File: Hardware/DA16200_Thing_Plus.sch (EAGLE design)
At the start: 60 parts, among them J2 THING_PLUS, J3 Qwiic, J5 USB C, J6 microSD, J7 CORTEX_JTAG_DEBUG_PTH_NS, Q1 20V/4.2A/52mΩ/1.4W, U1 DA16200MOD, U2 CH340E_MSOP10, U3 MCP73831, U7 3.3V

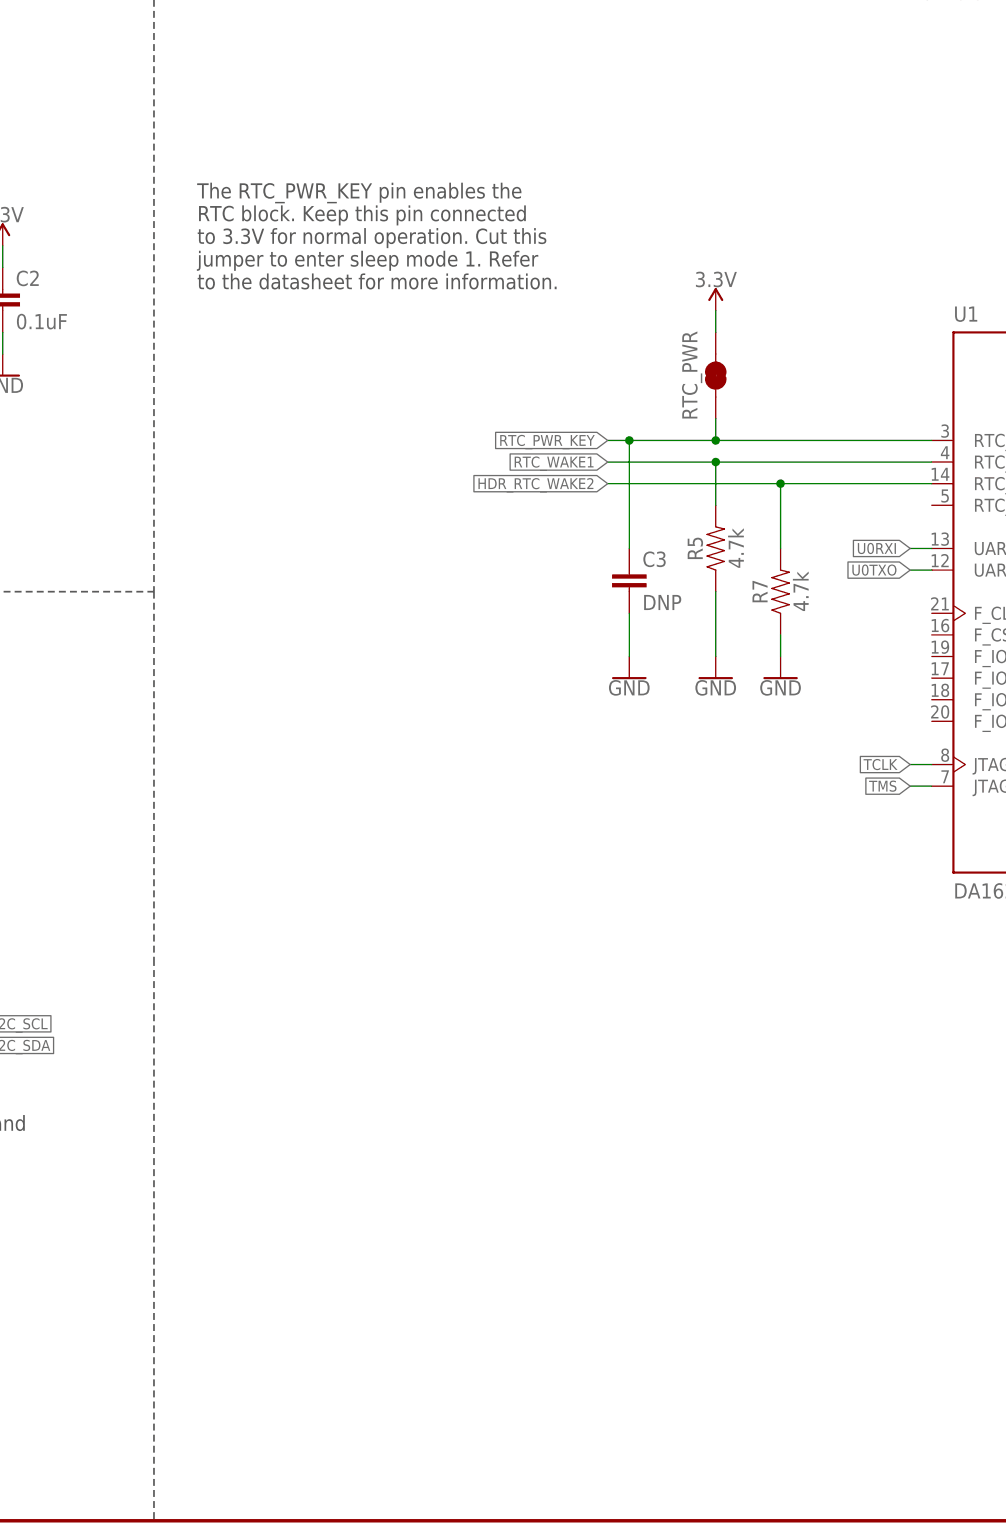
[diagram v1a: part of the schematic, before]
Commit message: Add SPDT switch for RTC_PWR_KEY
Added surface mount switch to pull RTC_PWR_KEY to 3.3V or GND
* Needed to extend the length of board by one grid space
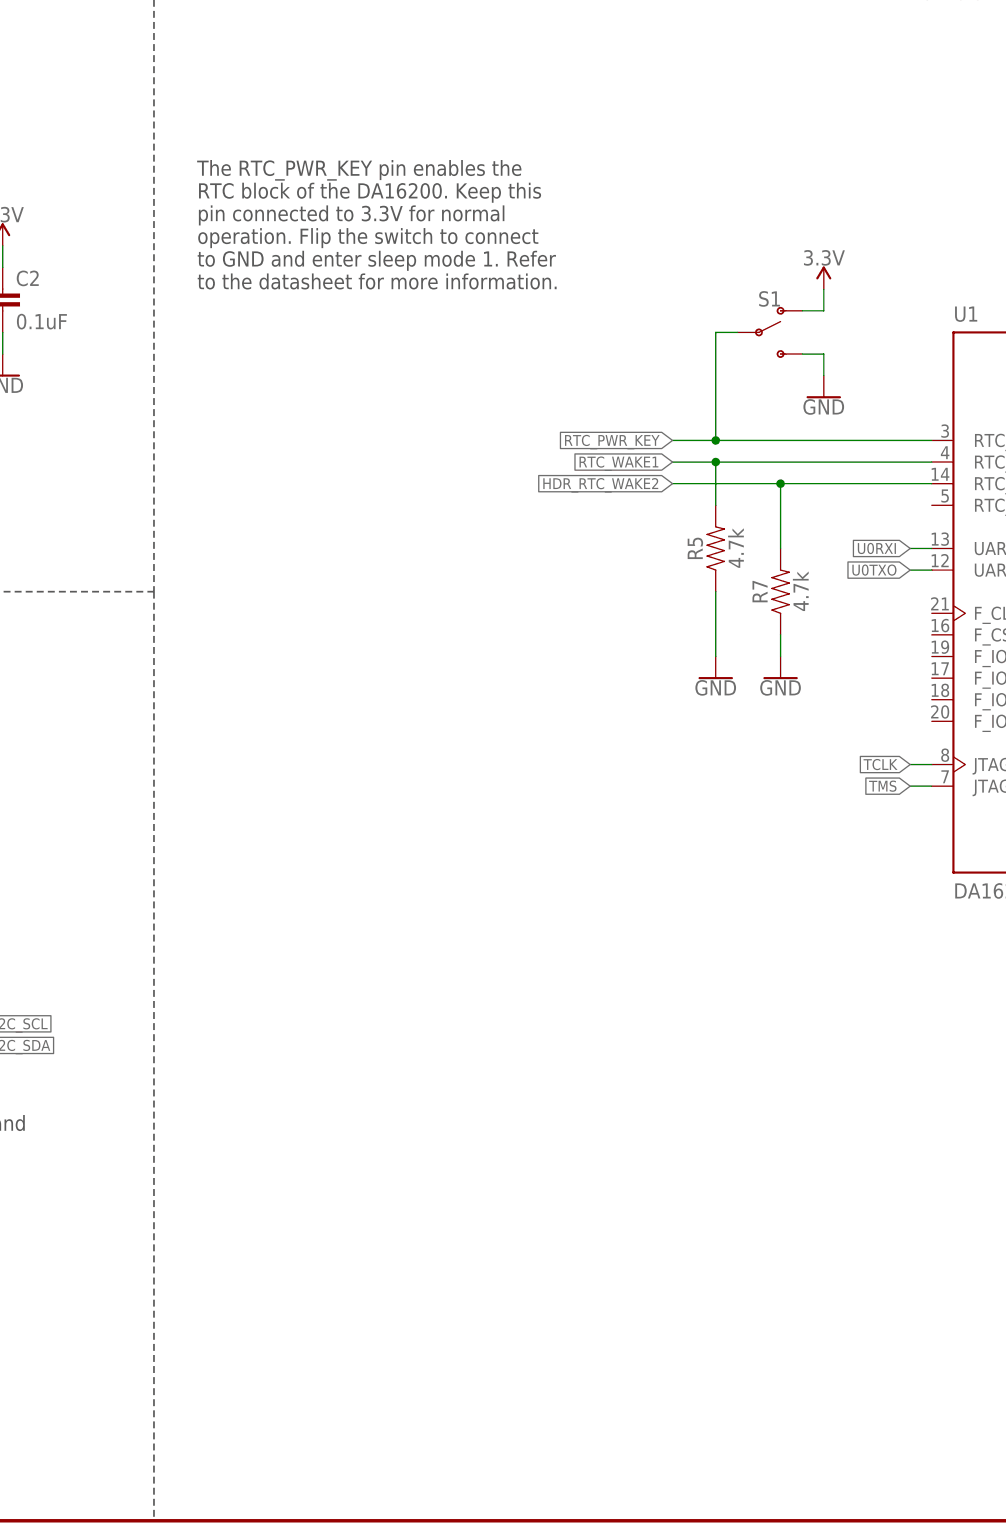
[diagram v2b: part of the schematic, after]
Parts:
- removed C3: DNP, SparkFun-Capacitors:DNP-0402-TIGHT
- removed RTC_PWR: JUMPER-SMT_2_NC_TRACE_SILK, SparkFun-Jumpers:JUMPER-SMT_2_NC_TRACE_SILK
- added S1: (no value), SparkFun-Switches:SWITCH-SPDT-SMD-AYZ0202
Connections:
- net 3.3V: now also S1.O; no longer RTC_PWR.2
- net GND: now also S1.S; no longer C3.2
- net RTC_PWR_KEY: now also S1.P; no longer C3.1, RTC_PWR.1
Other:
- note added: "The RTC_PWR_KEY pin enables the RTC block of the DA16200. Keep this pin connected to 3.3V for normal operation. Flip the switch to connect to GND and enter sleep mode 1. Refer to the datasheet for more information."
- note removed: "The RTC_PWR_KEY pin enables the RTC block. Keep this pin connected to 3.3V for normal operation. Cut this jumper to enter sleep mode 1. Refer to the datasheet for more information."
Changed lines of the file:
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@@
 <part name="R5" library="SparkFun-Resistors" deviceset="4.7KOHM" device="-0402T-1/16W-1%" value="4.7k"/>
 <part name="R7" library="SparkFun-Resistors" deviceset="4.7KOHM" device="-0402T-1/16W-1%" value="4.7k"/>
-<part name="C3" library="SparkFun-Capacitors" deviceset="DNP" device="-0402-TIGHT" value="DNP"/>
 <part name="GND17" library="SparkFun-PowerSymbols" deviceset="GND" device=""/>
 <part name="GND18" library="SparkFun-PowerSymbols" deviceset="GND" device=""/>
@@
 <part name="TMS" library="SparkFun-Connectors" deviceset="TEST-POINT" device="3"/>
 <part name="GPIOC7" library="SparkFun-Connectors" deviceset="TEST-POINT" device="3"/>
-<part name="RTC_PWR" library="SparkFun-Jumpers" deviceset="JUMPER-SMT_2_NC_TRACE" device="_SILK" package3d_urn="urn:adsk.eagle:package:39281/1"/>
+<part name="S1" library="SparkFun-Switches" deviceset="SWITCH-SPDT" device="-SMD-AYZ0202"/>
 </parts>
 <sheets>
@@
 <wire x1="261.62" y1="137.16" x2="330.2" y2="137.16" width="0.2032" layer="97" style="longdash"/>
 <wire x1="76.2" y1="190.5" x2="76.2" y2="109.22" width="0.2032" layer="97" style="longdash"/>
-<wire x1="76.2" y1="109.22" x2="76.2" y2="66.04" width="0.2032" layer="97" style="longdash"/>
-<wire x1="76.2" y1="66.04" x2="76.2" y2="0" width="0.2032" layer="97" style="longdash"/>
+<wire x1="76.2" y1="109.22" x2="76.2" y2="0" width="0.2032" layer="97" style="longdash"/>
 <wire x1="0" y1="109.22" x2="76.2" y2="109.22" width="0.2032" layer="97" style="longdash"/>
 <text x="172.974" y="180.086" size="2.54" layer="94" font="vector" align="center">DA16200 Module</text>
@@
 from power.</text>
 <text x="81.28" y="144.78" size="1.778" layer="97" font="vector">The RTC_PWR_KEY pin enables the
-RTC block. Keep this pin connected
-to 3.3V for normal operation. Cut this
-jumper to enter sleep mode 1. Refer
+RTC block of the DA16200. Keep this
+pin connected to 3.3V for normal
+operation. Flip the switch to connect
+to GND and enter sleep mode 1. Refer
 to the datasheet for more information.</text>
 </plain>
@@
 <attribute name="VALUE" x="151.384" y="109.22" size="1.778" layer="96" font="vector" rot="R90" align="top-center"/>
 </instance>
-<instance part="C3" gate="G$1" x="132.08" y="109.22" smashed="yes">
-<attribute name="NAME" x="133.604" y="112.141" size="1.778" layer="95" font="vector"/>
-<attribute name="VALUE" x="133.604" y="107.061" size="1.778" layer="96" font="vector"/>
-</instance>
-<instance part="GND17" gate="1" x="132.08" y="99.06" smashed="yes">
-<attribute name="VALUE" x="132.08" y="98.806" size="1.778" layer="96" align="top-center"/>
+<instance part="GND17" gate="1" x="154.94" y="132.08" smashed="yes">
+<attribute name="VALUE" x="154.94" y="131.826" size="1.778" layer="96" align="top-center"/>
 </instance>
 <instance part="GND18" gate="1" x="142.24" y="99.06" smashed="yes">
@@
 <attribute name="VALUE" x="149.86" y="98.806" size="1.778" layer="96" align="top-center"/>
 </instance>
-<instance part="SUPPLY8" gate="G$1" x="142.24" y="142.24" smashed="yes">
-<attribute name="VALUE" x="142.24" y="145.034" size="1.778" layer="96" align="bottom-center"/>
+<instance part="SUPPLY8" gate="G$1" x="154.94" y="144.78" smashed="yes">
+<attribute name="VALUE" x="154.94" y="147.574" size="1.778" layer="96" align="bottom-center"/>
 </instance>
 <instance part="LED" gate="G$1" x="281.94" y="109.22" smashed="yes" rot="R90">
@@
 <attribute name="NAME" x="312.42" y="152.4" size="1.778" layer="95" font="vector" rot="R270"/>
 </instance>
-<instance part="RTC_PWR" gate="G$1" x="142.24" y="134.62" smashed="yes" rot="R90">
-<attribute name="NAME" x="139.192" y="134.62" size="1.778" layer="95" font="vector" rot="R90" align="center"/>
+<instance part="S1" gate="1" x="147.32" y="139.7" smashed="yes">
+<attribute name="NAME" x="148.59" y="142.748" size="1.778" layer="95" font="vector" align="bottom-center"/>
+<attribute name="VALUE" x="148.336" y="136.398" size="1.778" layer="96" font="vector" align="top-center"/>
 </instance>
 </instances>
@@
 </segment>
 <segment>
-<pinref part="RTC_PWR" gate="G$1" pin="2"/>
+<pinref part="S1" gate="1" pin="O"/>
+<wire x1="152.4" y1="142.24" x2="154.94" y2="142.24" width="0.1524" layer="91"/>
 <pinref part="SUPPLY8" gate="G$1" pin="3.3V"/>
-<wire x1="142.24" y1="142.24" x2="142.24" y2="139.7" width="0.1524" layer="91"/>
+<wire x1="154.94" y1="142.24" x2="154.94" y2="144.78" width="0.1524" layer="91"/>
 </segment>
 </net>
@@
 </segment>
 <segment>
-<pinref part="C3" gate="G$1" pin="2"/>
-<pinref part="GND17" gate="1" pin="GND"/>
-<wire x1="132.08" y1="101.6" x2="132.08" y2="106.68" width="0.1524" layer="91"/>
-</segment>
-<segment>
 <pinref part="R5" gate="G$1" pin="1"/>
 <pinref part="GND18" gate="1" pin="GND"/>
@@
 <wire x1="317.5" y1="215.9" x2="317.5" y2="218.44" width="0.1524" layer="91"/>
 <pinref part="GND24" gate="1" pin="GND"/>
+</segment>
+<segment>
+<pinref part="S1" gate="1" pin="S"/>
+<wire x1="152.4" y1="137.16" x2="154.94" y2="137.16" width="0.1524" layer="91"/>
+<wire x1="154.94" y1="137.16" x2="154.94" y2="134.62" width="0.1524" layer="91"/>
+<pinref part="GND17" gate="1" pin="GND"/>
 </segment>
 </net>
@@
 <pinref part="U1" gate="G$1" pin="RTC_PWR_KEY"/>
 <wire x1="167.64" y1="127" x2="142.24" y2="127" width="0.1524" layer="91"/>
-<wire x1="142.24" y1="127" x2="132.08" y2="127" width="0.1524" layer="91"/>
-<wire x1="132.08" y1="127" x2="129.54" y2="127" width="0.1524" layer="91"/>
-<label x="129.54" y="127" size="1.27" layer="95" rot="R180" xref="yes"/>
-<pinref part="C3" gate="G$1" pin="1"/>
-<wire x1="132.08" y1="114.3" x2="132.08" y2="127" width="0.1524" layer="91"/>
-<junction x="132.08" y="127"/>
-<pinref part="RTC_PWR" gate="G$1" pin="1"/>
-<wire x1="142.24" y1="129.54" x2="142.24" y2="127" width="0.1524" layer="91"/>
+<wire x1="142.24" y1="127" x2="137.16" y2="127" width="0.1524" layer="91"/>
+<label x="137.16" y="127" size="1.27" layer="95" rot="R180" xref="yes"/>
+<wire x1="142.24" y1="127" x2="142.24" y2="139.7" width="0.1524" layer="91"/>
 <junction x="142.24" y="127"/>
+<pinref part="S1" gate="1" pin="P"/>
+<wire x1="142.24" y1="139.7" x2="144.78" y2="139.7" width="0.1524" layer="91"/>
 </segment>
 <segment>
@@
 <pinref part="U1" gate="G$1" pin="RTC_WAKE_UP"/>
 <wire x1="167.64" y1="124.46" x2="142.24" y2="124.46" width="0.1524" layer="91"/>
-<label x="129.54" y="124.46" size="1.27" layer="95" rot="R180" xref="yes"/>
+<label x="137.16" y="124.46" size="1.27" layer="95" rot="R180" xref="yes"/>
 <pinref part="R5" gate="G$1" pin="2"/>
-<wire x1="142.24" y1="124.46" x2="129.54" y2="124.46" width="0.1524" layer="91"/>
+<wire x1="142.24" y1="124.46" x2="137.16" y2="124.46" width="0.1524" layer="91"/>
 <wire x1="142.24" y1="119.38" x2="142.24" y2="124.46" width="0.1524" layer="91"/>
 <junction x="142.24" y="124.46"/>
@@
 <pinref part="U1" gate="G$1" pin="RTC_WAKE_UP2"/>
 <wire x1="167.64" y1="121.92" x2="149.86" y2="121.92" width="0.1524" layer="91"/>
-<wire x1="149.86" y1="121.92" x2="129.54" y2="121.92" width="0.1524" layer="91"/>
+<wire x1="149.86" y1="121.92" x2="137.16" y2="121.92" width="0.1524" layer="91"/>
 <pinref part="R7" gate="G$1" pin="2"/>
 <wire x1="149.86" y1="121.92" x2="149.86" y2="114.3" width="0.1524" layer="91"/>
 <junction x="149.86" y="121.92"/>
-<label x="129.54" y="121.92" size="1.27" layer="95" rot="R180" xref="yes"/>
-</segment>
-<segment>
+<label x="137.16" y="121.92" size="1.27" layer="95" rot="R180" xref="yes"/>
+</segment>
+<segment>

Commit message: Add uSD friction fit to schematic
* Renamed net labels to match connecting to the uSD socket defined by UM-WI-046 pg 30
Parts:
- added J1: MICRO-SDFRICTION, SparkFun-Connectors:MICRO-SDFRICTION
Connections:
- removed net !RESET!/SPI_CLK: J2.!RESET, J2.SCK, J6.CLK/SCK, R13.2, U1.GPIOA7
- removed net SPI_CSB: J2.GPIO6, R20.1, U1.GPIOA6
- removed net SPI_PICO: J2.PICO, J6.CMD/SDI, U1.GPIOA8
- removed net SPI_POCI: J2.POCI, J6.DAT0/SDO, U1.GPIOA9
- removed net U1RXI: J2.RX, U1.GPIOA5
- removed net U1TXO: J2.TX, U1.GPIOA4
- new net !RESET!/SPI_CLK/SD_D2: J1.DAT2, J2.!RESET, J2.SCK, J6.CLK/SCK, R13.2, U1.GPIOA7
- new net SPI_CSB/SD_D3: J1.DAT3/!CS!, J2.GPIO6, R20.1, U1.GPIOA6
- new net SPI_PICO/SD_D1: J1.DAT1, J2.PICO, J6.CMD/SDI, U1.GPIOA8
- new net SPI_POCI/SD_D0: J1.DAT0/SDO, J2.POCI, J6.DAT0/SDO, U1.GPIOA9
- new net U1RXI/SD_CLK: J1.CLK/SCK, J2.RX, U1.GPIOA5
- new net U1TXO/SD_CMD: J1.CMD/SDI, J2.TX, U1.GPIOA4
- net 3.3V: now also J1.VCC; no longer J6.VCC
- net GND: now also J1.GND; no longer J6.GND, J6.SHIELD
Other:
- moved on the sheet: R20, R5, R7, S1, U1
